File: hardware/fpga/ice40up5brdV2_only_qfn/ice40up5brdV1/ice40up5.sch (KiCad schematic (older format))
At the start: 3 parts, among them U1 ICE40UP5K-SG48ITR

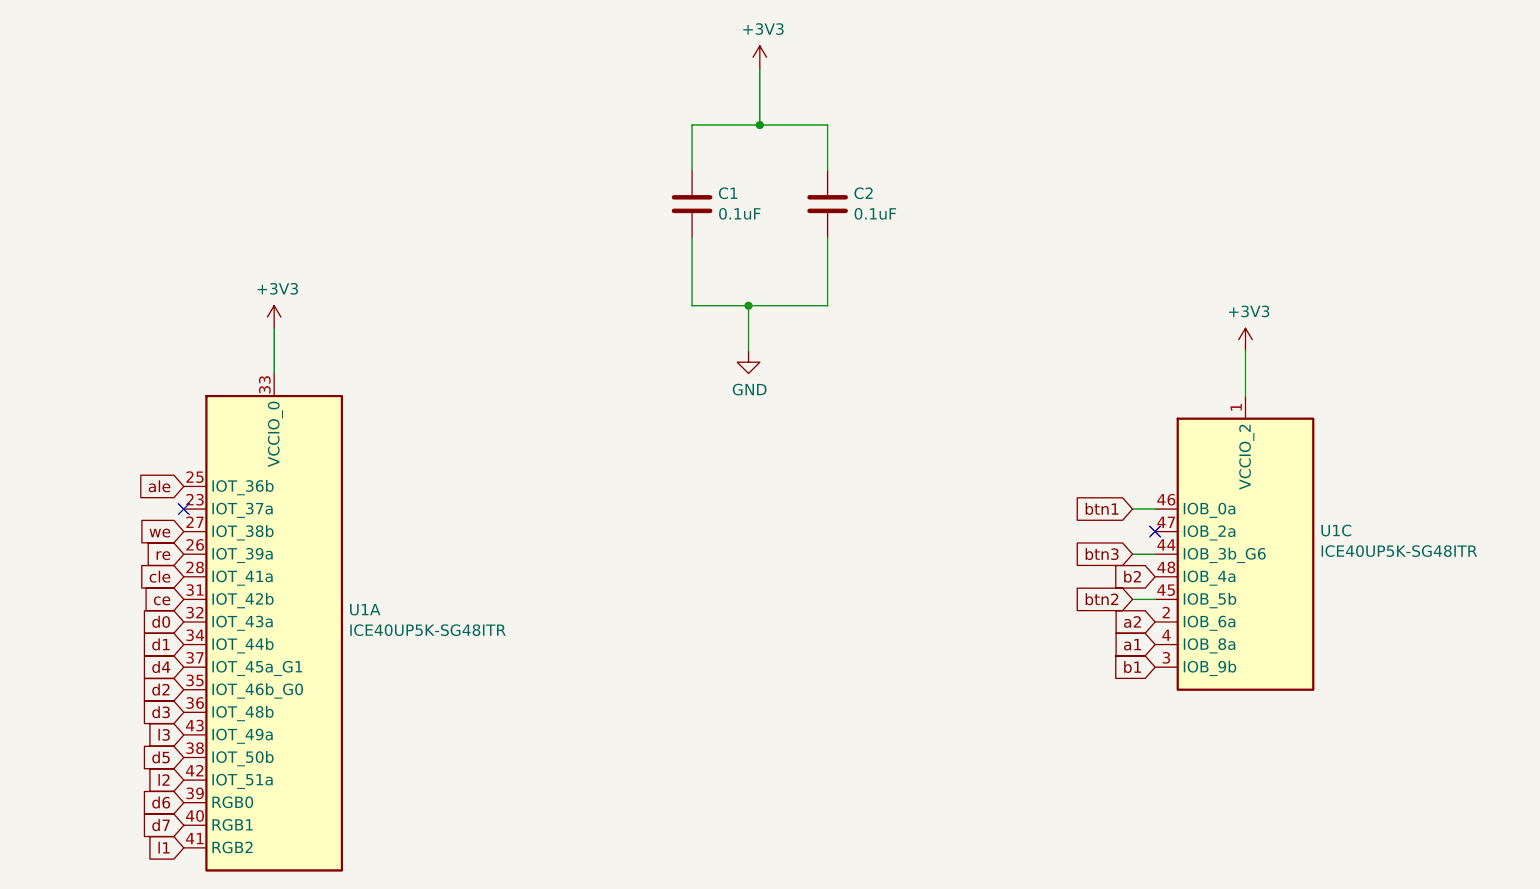
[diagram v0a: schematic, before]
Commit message: ice40qfn 4layer board started
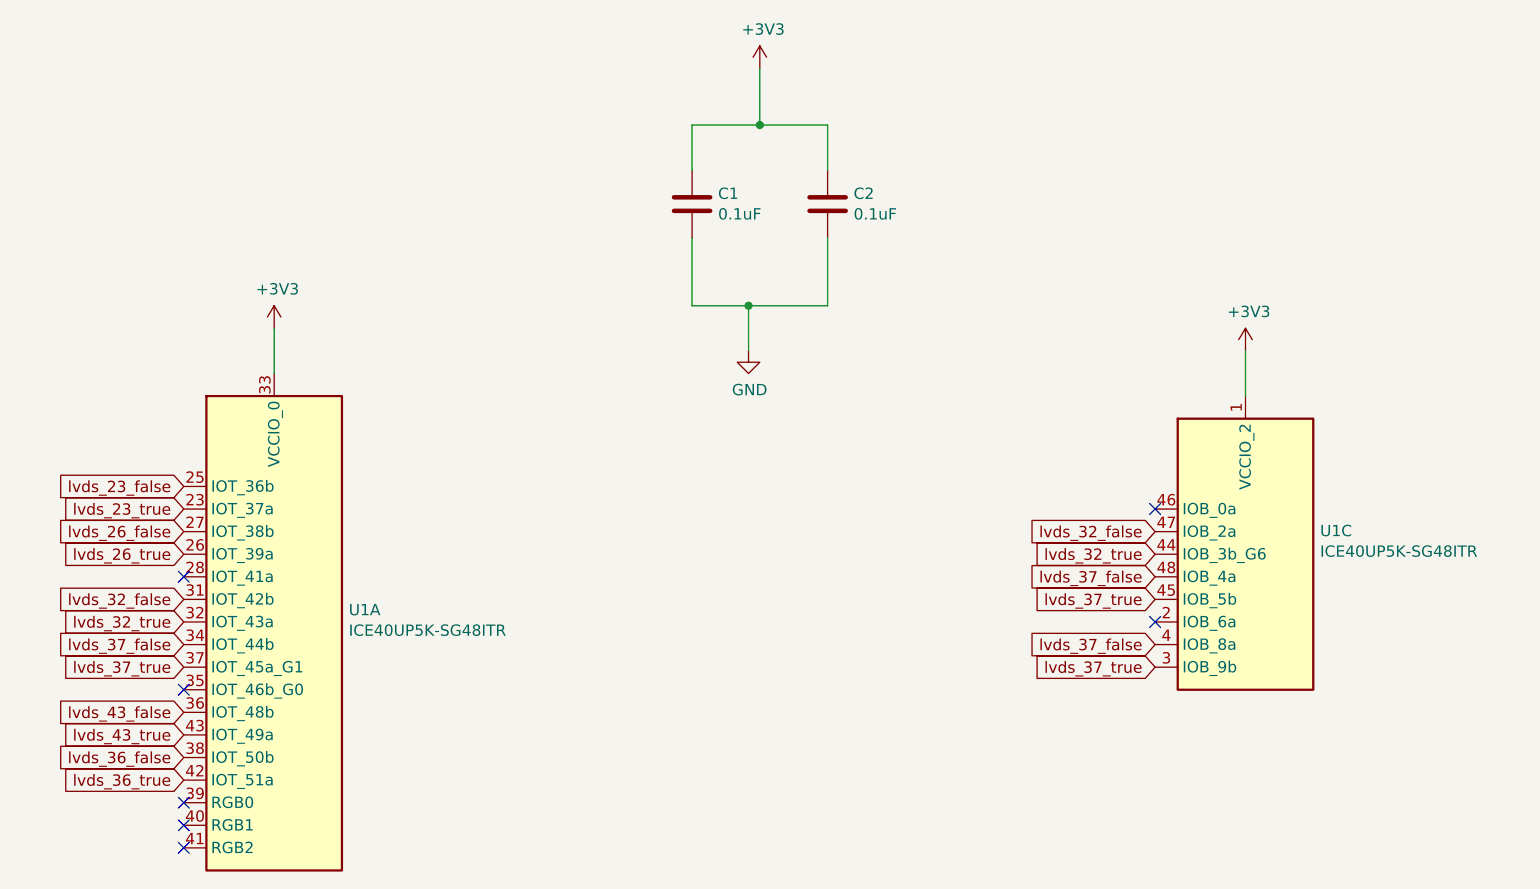
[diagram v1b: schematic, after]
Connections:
- net b2 is gone; now on net lvds_37_false: U1.48 (IOB_4a)
- net btn2 is gone; now on net lvds_37_true: U1.45 (IOB_5b)
- net ce is gone; now on net lvds_32_false: U1.31 (IOT_42b)
- net d0 is gone; now on net lvds_32_true: U1.32 (IOT_43a)
- net d1 is gone; now on net lvds_37_false: U1.34 (IOT_44b)
- net d4 is gone; now on net lvds_37_true: U1.37 (IOT_45a_G1)
- net lvds_23_true: now reaches U1.23 (IOT_37a)
- net lvds_32_false: now reaches U1.47 (IOB_2a)
- net a1 renamed lvds_37_false
- net a2: no longer names the net of U1.2 (IOB_6a)
- net ale renamed lvds_23_false
- net b1 renamed lvds_37_true
- net btn1: no longer names the net of U1.46 (IOB_0a)
- net btn3 renamed lvds_32_true
- net cle: no longer names the net of U1.28 (IOT_41a)
- net d2: no longer names the net of U1.35 (IOT_46b_G0)
- net d3 renamed lvds_43_false
- net d5 renamed lvds_36_false
- net d6: no longer names the net of U1.39 (RGB0)
- net d7: no longer names the net of U1.40 (RGB1)
- net l1: no longer names the net of U1.41 (RGB2)
- net l2 renamed lvds_36_true
- net l3 renamed lvds_43_true
- net re renamed lvds_26_true
- net we renamed lvds_26_false
- no-connect marks 2 -> 7
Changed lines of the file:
@@
 $EndComp
 Text GLabel 2750 3200 0    50   Input ~ 0
-ale
-Text GLabel 2750 3500 0    50   Input ~ 0
-re
-Text GLabel 2750 3400 0    50   Input ~ 0
-we
-Text GLabel 2750 3600 0    50   Input ~ 0
-cle
-Text GLabel 2750 3700 0    50   Input ~ 0
-ce
-Text GLabel 2750 3800 0    50   Input ~ 0
-d0
-Text GLabel 2750 3900 0    50   Input ~ 0
-d1
-Text GLabel 2750 4100 0    50   Input ~ 0
-d2
-Text GLabel 2750 4200 0    50   Input ~ 0
-d3
-Text GLabel 2750 4000 0    50   Input ~ 0
-d4
-Text GLabel 2750 4400 0    50   Input ~ 0
-d5
-Text GLabel 2750 4600 0    50   Input ~ 0
-d6
-Text GLabel 2750 4700 0    50   Input ~ 0
-d7
-Text GLabel 7050 3900 0    50   Input ~ 0
-a1
-Text GLabel 7050 4000 0    50   Input ~ 0
-b1
-Text GLabel 7050 3800 0    50   Input ~ 0
-a2
-Text GLabel 7050 3600 0    50   Input ~ 0
-b2
+lvds_23_false
 $Comp
 L power:+3V3 #PWR01
@@
 Wire Wire Line
 	5250 2400 5600 2400
-NoConn ~ 2750 3300
-Text GLabel 2750 4800 0    50   Input ~ 0
-l1
+Text GLabel 2750 3300 0    50   Input ~ 0
+lvds_23_true
+Text GLabel 2750 3400 0    50   Input ~ 0
+lvds_26_false
+Text GLabel 2750 3500 0    50   Input ~ 0
+lvds_26_true
+Text GLabel 2750 3700 0    50   Input ~ 0
+lvds_32_false
+Text GLabel 2750 3800 0    50   Input ~ 0
+lvds_32_true
+NoConn ~ 2750 3600
+Text GLabel 2750 3900 0    50   Input ~ 0
+lvds_37_false
+Text GLabel 2750 4000 0    50   Input ~ 0
+lvds_37_true
+NoConn ~ 2750 4100
+NoConn ~ 2750 4600
+NoConn ~ 2750 4700
+NoConn ~ 2750 4800
+Text GLabel 2750 4200 0    50   Input ~ 0
+lvds_43_false
+Text GLabel 2750 4300 0    50   Input ~ 0
+lvds_43_true
+Text GLabel 2750 4400 0    50   Input ~ 0
+lvds_36_false
 Text GLabel 2750 4500 0    50   Input ~ 0
-l2
-Text GLabel 2750 4300 0    50   Input ~ 0
-l3
-Text GLabel 6950 3300 0    50   Input ~ 0
-btn1
-Wire Wire Line
-	6950 3300 7050 3300
-Text GLabel 6950 3700 0    50   Input ~ 0
-btn2
-Wire Wire Line
-	6950 3700 7050 3700
-Text GLabel 6950 3500 0    50   Input ~ 0
-btn3
-Wire Wire Line
-	6950 3500 7050 3500
-NoConn ~ 7050 3400
+lvds_36_true
+NoConn ~ 7050 3300
+Text GLabel 7050 3400 0    50   Input ~ 0
+lvds_32_false
+Text GLabel 7050 3500 0    50   Input ~ 0
+lvds_32_true
+Text GLabel 7050 3600 0    50   Input ~ 0
+lvds_37_false
+Text GLabel 7050 3700 0    50   Input ~ 0
+lvds_37_true
+NoConn ~ 7050 3800
+Text GLabel 7050 3900 0    50   Input ~ 0
+lvds_37_false
+Text GLabel 7050 4000 0    50   Input ~ 0
+lvds_37_true
 $EndSCHEMATC
